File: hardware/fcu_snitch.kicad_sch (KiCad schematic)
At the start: 41 parts, among them J2 02x03_JST_SWD, J3 Conn_02x04_Top_Bottom, J4 Conn_01x02_Socket, J5 Conn_01x04_Socket, Q1 NPN, U4 LPS22HBTR, U5 LSM6DSO32

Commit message: schematic update and pcb route v1
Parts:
- removed R23: R, Resistor_SMD:R_0805_2012Metric, symbol Device:R
- added R13, R14: R_Small_US, Resistor_SMD:R_0805_2012Metric, symbol Device:R_Small_US
- Q1: footprint Package_TO_SOT_THT:TO-92_Inline -> Package_TO_SOT_SMD:SOT-23; symbol Transistor_BJT:S8050 -> Transistor_BJT:MMBTA06
- renumbered C47 to C1, C46 to C2, C38 to C3, C45 to C4, D6 to D2, D7 to D3, D8 to D6, J4 to J1, J3 to J2, J5 to J3, J2 to J4, R22 to R1, R13 to R10, R14 to R11, R7 to R12, R5 to R16, R16 to R17, R17 to R18, R21 to R19, R9 to R2, R26 to R20, R25 to R21, R6 to R22, R24 to R23, R3 to R24, R18 to R3, R8 to R4, R10 to R5, R11 to R6, R12 to R7, R19 to R8, R20 to R9, U5 to U1, U4 to U2
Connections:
- net VDD is gone; now on net +3.3V: R19.1
- net +3.3V: now also U2.6 (CS), R13.2
- net GND: now also Q1.2 (E), R14.2; no longer Q1.1 (E)
- net STM32WLE5 + Radio/SPI2_{CS}: now also R13.1, R14.1
- net STM32WLE5 + Radio/SPI2_{MISO}: no longer D4.3 (K)
- net at J3.2 (Pin_2), R15.2: now also D4.3 (K)
- net RTS: now reaches D3.4 (K), J2.7 (Pin_7), R6.2
- net CK: now reaches D3.5 (K), J2.8 (Pin_8), R7.2
- net TX1: now reaches D2.3 (K), J2.3 (Pin_3), R11.2
- net RX1: now reaches D2.4 (K), J2.2 (Pin_2), R10.2
- net at R22.2: now also Q1.1 (B); no longer Q1.2 (B)
- net CTS: now reaches D3.3 (K), J2.6 (Pin_6), R5.2
- net STM32WLE5 + Radio/VMONITOR renamed VMON
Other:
- moved on the sheet: D4, J3, R17, R18

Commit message: better pcb route (no test pads)
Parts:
- removed R8: R_Small_US, Resistor_SMD:R_0805_2012Metric, symbol Device:R_Small_US
- added H1, H2, H3, H4: MountingHole, MountingHole:MountingHole_2.2mm_M2, symbol Mechanical:MountingHole
- added R16: R_Small_US, Resistor_SMD:R_0805_2012Metric, symbol Device:R_Small_US
- C1: renamed from C2; KiLib_Generator (none) -> SMD_2terminal_chip_molded
- C2: renamed from C1; KiLib_Generator (none) -> SMD_2terminal_chip_molded
- C23: renamed from C3; KiLib_Generator (none) -> SMD_2terminal_chip_molded
- C3: renamed from C4; KiLib_Generator (none) -> SMD_2terminal_chip_molded
- D2, D3, D4, Q1: KiLib_Generator (none) -> package/gullwing
- D7: renamed from D6; KiLib_Generator (none) -> package/gullwing
- J1: renamed from J3; KiLib_Generator (none) -> connector/JST
- J2: renamed from J1; KiLib_Generator (none) -> connector/JST
- J3: renamed from J2; KiLib_Generator (none) -> connector/JST
- J5: renamed from J4; KiLib_Generator (none) -> connector/pin_header_socket
- R1: renamed from R2; KiLib_Generator (none) -> SMD_2terminal_chip_molded
- R10: renamed from R7; KiLib_Generator (none) -> SMD_2terminal_chip_molded
- R11: renamed from R5; KiLib_Generator (none) -> SMD_2terminal_chip_molded
- R12: renamed from R6; KiLib_Generator (none) -> SMD_2terminal_chip_molded
- R13: renamed from R11; KiLib_Generator (none) -> SMD_2terminal_chip_molded
- R14: renamed from R9; KiLib_Generator (none) -> SMD_2terminal_chip_molded
- R15: renamed from R3; KiLib_Generator (none) -> SMD_2terminal_chip_molded
- R17: renamed from R21; KiLib_Generator (none) -> SMD_2terminal_chip_molded
- R18: renamed from R23; KiLib_Generator (none) -> SMD_2terminal_chip_molded
- R19: renamed from R18; KiLib_Generator (none) -> SMD_2terminal_chip_molded
- R2: renamed from R4; KiLib_Generator (none) -> SMD_2terminal_chip_molded
- R21: renamed from R17; KiLib_Generator (none) -> SMD_2terminal_chip_molded
- R22: KiLib_Generator (none) -> SMD_2terminal_chip_molded
- R23: renamed from R24; KiLib_Generator (none) -> SMD_2terminal_chip_molded
- R26: renamed from R19; KiLib_Generator (none) -> SMD_2terminal_chip_molded
- R27: renamed from R20; KiLib_Generator (none) -> SMD_2terminal_chip_molded
- R3: renamed from R12; KiLib_Generator (none) -> SMD_2terminal_chip_molded
- R4: renamed from R14; KiLib_Generator (none) -> SMD_2terminal_chip_molded
- R5: renamed from R16; KiLib_Generator (none) -> SMD_2terminal_chip_molded
- R6: renamed from R15; KiLib_Generator (none) -> SMD_2terminal_chip_molded
- R7: renamed from R13; KiLib_Generator (none) -> SMD_2terminal_chip_molded
- R8: renamed from R1; KiLib_Generator (none) -> SMD_2terminal_chip_molded
- R9: renamed from R10; KiLib_Generator (none) -> SMD_2terminal_chip_molded
- renumbered D5 to D6
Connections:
- net CTS: now also J3.5 (Pin_5); no longer J3.6 (Pin_6)
- net GND: now also J3.6 (Pin_6); no longer J3.5 (Pin_5)
- net STM32WLE5 + Radio/IMU_{MOSI}: now also R16.2
- net TX1: now also J3.4 (Pin_4); no longer J3.3 (Pin_3)
- net TX2: now reaches J2.1 (Pin_1), R1.2
- net TX2: now also D1.1; no longer D1.2
- net RX2: now reaches J2.2 (Pin_2), R2.2
- net RX2: now also D1.2; no longer D1.1
- net IMU_MOSI: now reaches U1.14 (SDA)
- net IMU_MOSI: now also R16.1
- net SPI2MISO: now reaches D4.3 (K), J1.2 (Pin_2), R6.2
- net at D2.1 (K), R3.2: now also J3.3 (Pin_3); no longer J3.4 (Pin_4)
- net SPI2MOSI: now reaches D4.4 (K), J1.3 (Pin_3), R21.2
- net SPI2SCK: now reaches D4.5 (K), J1.4 (Pin_4), R19.2
- net IMU_MISO: now reaches R14.1, U1.1 (SDO/SA0)
- net IMU_SCK: now reaches R15.1, U1.13 (SCL)
- net STM32WLE5 + Radio/IMU_{CS} renamed IMU_CS
- net STM32WLE5 + Radio/IMU_{INT} renamed IMU_INT
- net STM32WLE5 + Radio/SPI2_{CS} renamed SPI2CS
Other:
- moved on the sheet: R14, R15

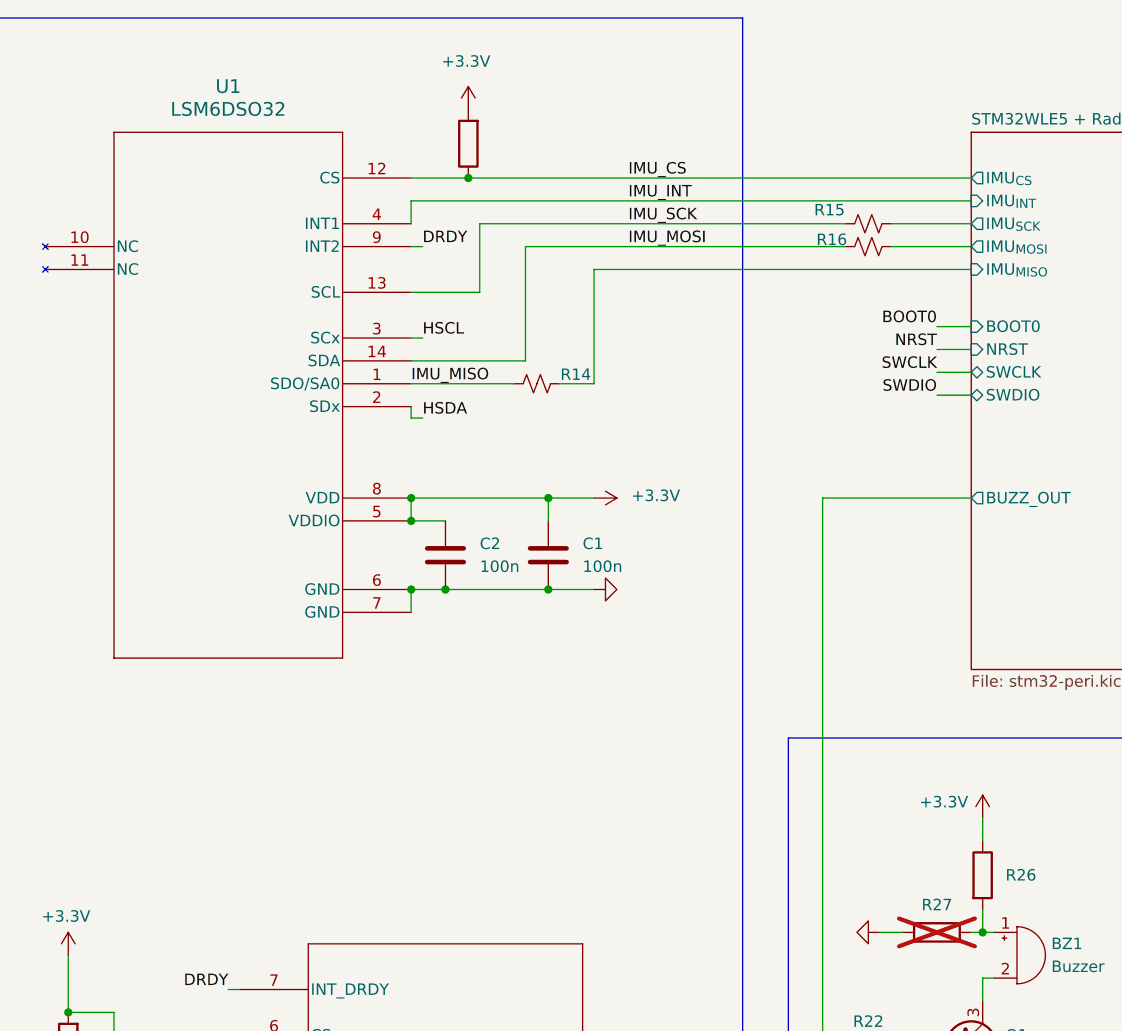
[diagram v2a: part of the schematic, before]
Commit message: pcb v2 update: test points, stickers, labeling
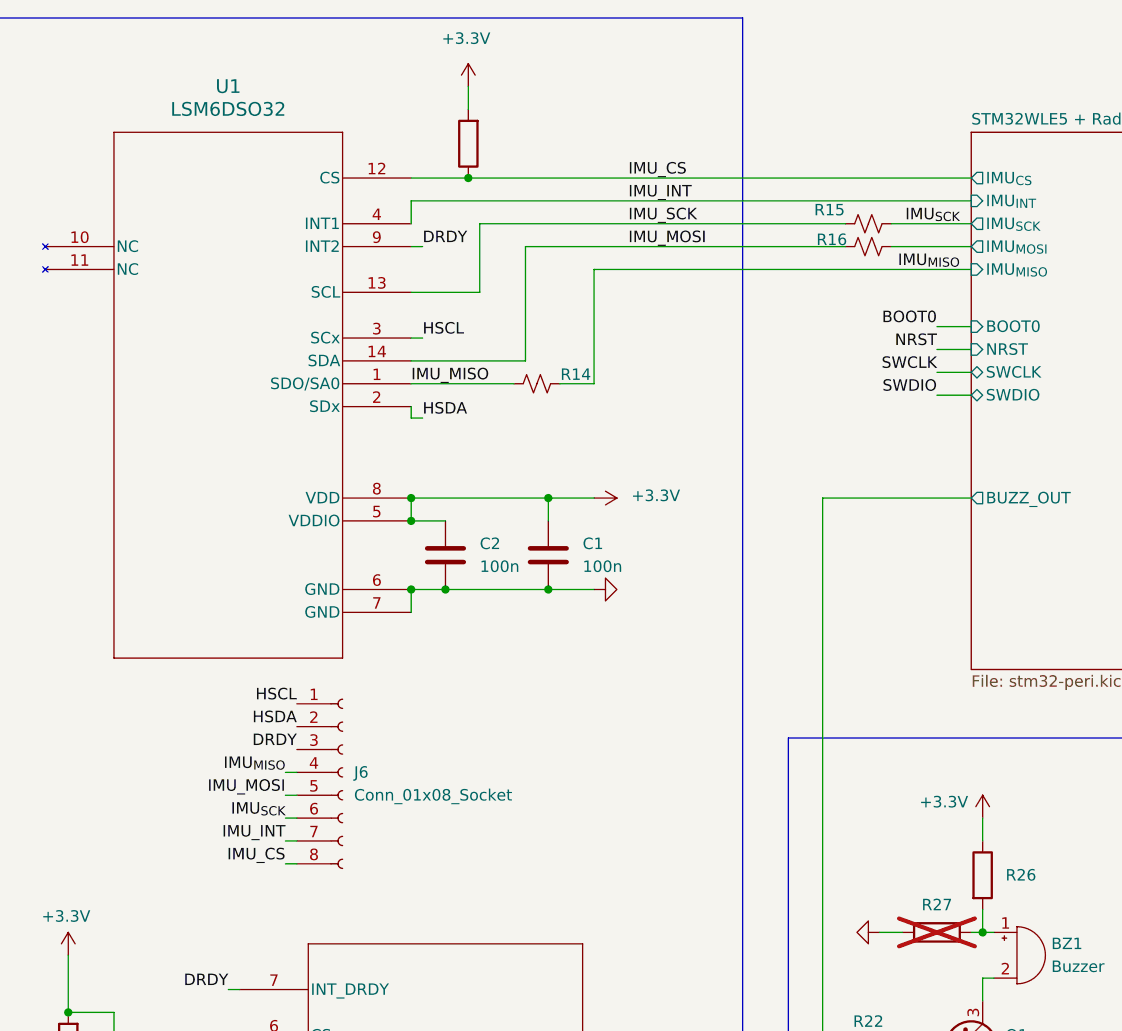
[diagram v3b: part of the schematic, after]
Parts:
- added J6: Conn_01x08_Socket, Connector_PinHeader_1.00mm:PinHeader_1x08_P1.00mm_Horizontal, symbol Connector:Conn_01x08_Socket
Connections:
- net DRDY: now also J6.3 (Pin_3)
- net HSCL: now also J6.1 (Pin_1)
- net HSDA: now also J6.2 (Pin_2)
- net IMU_CS: now also J6.8 (Pin_8)
- net IMU_INT: now also J6.7 (Pin_7)
- net IMU_MOSI: now also J6.5 (Pin_5)
- net STM32WLE5 + Radio/IMU_{MISO} renamed IMU_{MISO}
- net IMU_{MISO}: now also J6.4 (Pin_4)
- net STM32WLE5 + Radio/IMU_{SCK} renamed IMU_{SCK}
- net IMU_{SCK}: now also J6.6 (Pin_6)
